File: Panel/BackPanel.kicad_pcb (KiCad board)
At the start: 2 copper layers, 0 parts

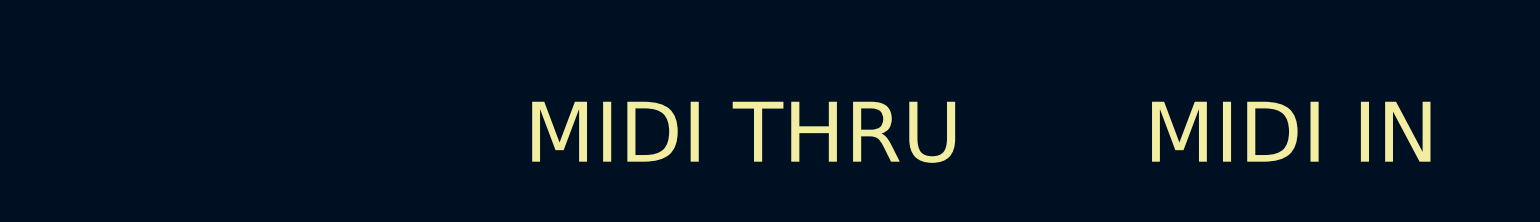
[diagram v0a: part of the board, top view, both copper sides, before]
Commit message: Exported DXFs, added more screw holes
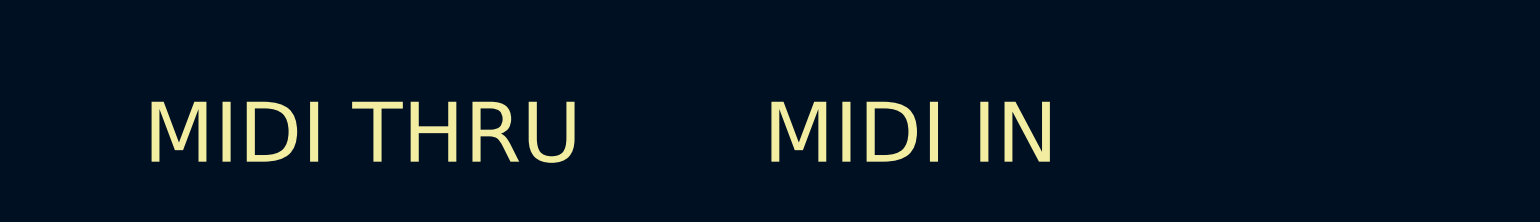
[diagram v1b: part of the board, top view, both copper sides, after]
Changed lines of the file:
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@@
   (general
     (thickness 1.6)
-    (drawings 23)
+    (drawings 26)
     (tracks 0)
     (zones 0)
@@
     (pad_to_mask_clearance 0.05)
     (aux_axis_origin 0 0)
+    (grid_origin 19.05 50.8)
     (visible_elements 7FFFFFFF)
     (pcbplotparams
-      (layerselection 0x010fc_ffffffff)
+      (layerselection 0x000a0_7ffffffe)
       (usegerberextensions false)
       (usegerberattributes true)
@@
       (padsonsilk false)
       (subtractmaskfromsilk false)
-      (outputformat 1)
+      (outputformat 3)
       (mirror false)
-      (drillshape 1)
+      (drillshape 0)
       (scaleselection 1)
-      (outputdirectory ""))
+      (outputdirectory "dxf/"))
   )
   (net 0 "")
@@
     (uvia_drill 0.1)
   )
-  (gr_text "MIDI THRU" (at 228.6 165.1) (layer F.SilkS)
+  (gr_circle (center 158.7 203.2) (end 160.7 203.2) (layer F.Mask) (width 0.15))
+  (gr_circle (center 279.35 203.2) (end 281.35 203.2) (layer F.Mask) (width 0.15))
+  (gr_circle (center 279.35 63.5) (end 281.35 63.5) (layer F.Mask) (width 0.15))
+  (gr_circle (center 527.05 63.5) (end 529.05 63.5) (layer F.Mask) (width 0.15))
+  (gr_circle (center 527.05 203.2) (end 529.05 203.2) (layer F.Mask) (width 0.15))
+  (gr_circle (center 31.75 201.7) (end 33.75 201.7) (layer F.Mask) (width 0.15))
+  (gr_circle (center 31.75 63.5) (end 33.75 63.5) (layer F.Mask) (width 0.15))
+  (gr_text "MIDI THRU" (at 196.85 165.1) (layer F.SilkS)
     (effects (font (size 5 5) (thickness 0.5)))
   )
-  (gr_text "MIDI IN" (at 274.32 165.1) (layer F.SilkS)
+  (gr_text "MIDI IN" (at 242.57 165.1) (layer F.SilkS)
     (effects (font (size 5 5) (thickness 0.5)))
   )
-  (gr_circle (center 239.85 180.34) (end 241.45 180.34) (layer F.Mask) (width 0.15))
-  (gr_circle (center 217.35 180.34) (end 218.95 180.34) (layer F.Mask) (width 0.15))
-  (gr_circle (center 228.6 180.34) (end 236.1 180.34) (layer F.Mask) (width 0.15))
-  (gr_circle (center 285.57 180.34) (end 287.17 180.34) (layer F.Mask) (width 0.15))
-  (gr_circle (center 263.07 180.34) (end 264.67 180.34) (layer F.Mask) (width 0.15))
-  (gr_circle (center 274.32 180.34) (end 281.82 180.34) (layer F.Mask) (width 0.15))
+  (gr_circle (center 208.1 180.34) (end 209.7 180.34) (layer F.Mask) (width 0.15))
+  (gr_circle (center 185.6 180.34) (end 187.2 180.34) (layer F.Mask) (width 0.15))
+  (gr_circle (center 196.85 180.34) (end 204.35 180.34) (layer F.Mask) (width 0.15))
+  (gr_circle (center 253.82 180.34) (end 255.42 180.34) (layer F.Mask) (width 0.15))
+  (gr_circle (center 231.32 180.34) (end 232.92 180.34) (layer F.Mask) (width 0.15))
+  (gr_circle (center 242.57 180.34) (end 250.07 180.34) (layer F.Mask) (width 0.15))
   (gr_circle (center 53.64 179.38) (end 55.39 179.38) (layer F.Mask) (width 0.15))
   (gr_circle (center 98.34 179.38) (end 100.09 179.38) (layer F.Mask) (width 0.15))
@@
     (effects (font (size 5 5) (thickness 0.5)))
   )
-  (gr_circle (center 527.05 63.5) (end 528.55 63.5) (layer F.Mask) (width 0.15))
-  (gr_circle (center 527.05 203.2) (end 528.55 203.2) (layer F.Mask) (width 0.15))
-  (gr_circle (center 31.75 201.7) (end 33.25 201.7) (layer F.Mask) (width 0.15))
-  (gr_circle (center 31.75 63.5) (end 33.25 63.5) (layer F.Mask) (width 0.15))
   (gr_line (start 19.05 215.9) (end 19.05 50.8) (layer F.Mask) (width 0.15))
   (gr_line (start 539.75 215.9) (end 19.05 215.9) (layer F.Mask) (width 0.15))

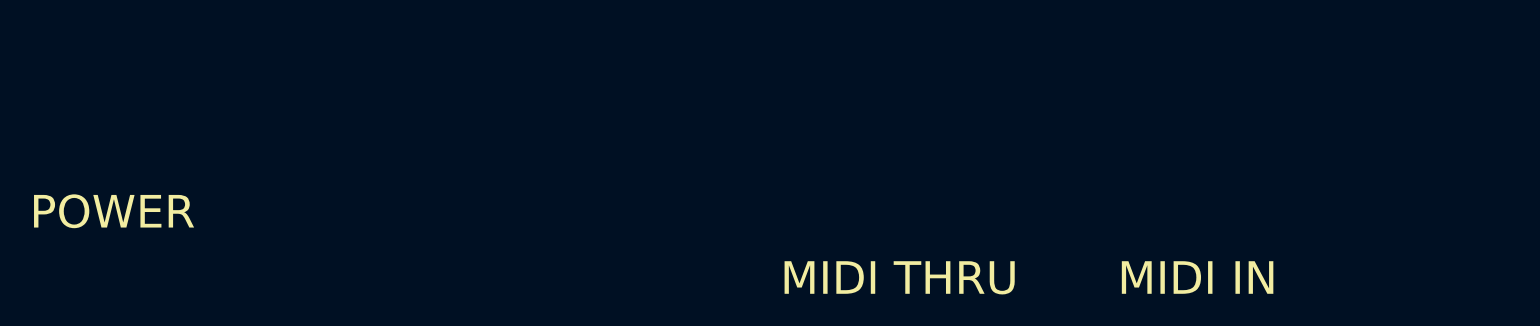
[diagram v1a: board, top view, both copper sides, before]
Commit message: Exported panel, fixed missing net on filter
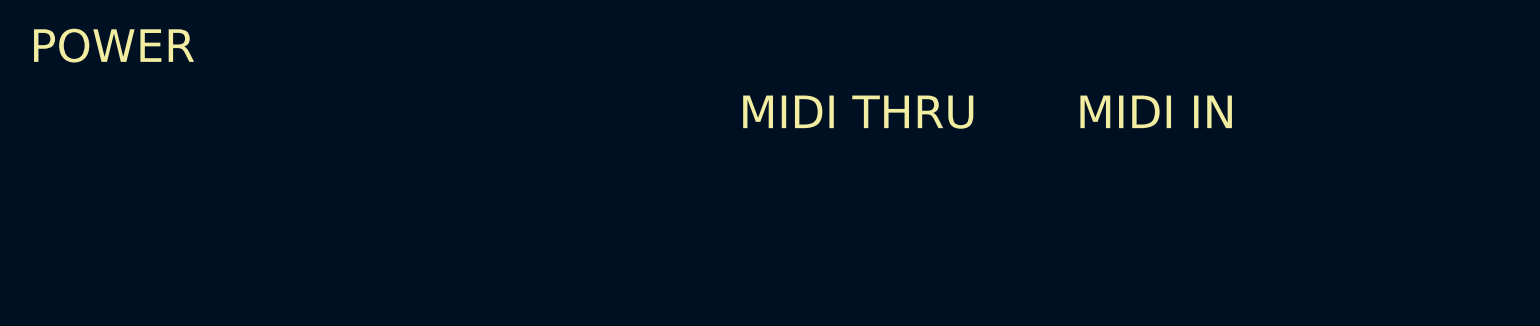
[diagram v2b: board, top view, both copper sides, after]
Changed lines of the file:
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@@
   (general
     (thickness 1.6)
-    (drawings 26)
+    (drawings 28)
     (tracks 0)
     (zones 0)
@@
       (padsonsilk false)
       (subtractmaskfromsilk false)
-      (outputformat 3)
+      (outputformat 5)
       (mirror false)
       (drillshape 0)
       (scaleselection 1)
-      (outputdirectory "dxf/"))
+      (outputdirectory "svg/"))
   )
   (net 0 "")
@@
     (uvia_drill 0.1)
   )
-  (gr_circle (center 158.7 203.2) (end 160.7 203.2) (layer F.Mask) (width 0.15))
-  (gr_circle (center 279.35 203.2) (end 281.35 203.2) (layer F.Mask) (width 0.15))
-  (gr_circle (center 279.35 63.5) (end 281.35 63.5) (layer F.Mask) (width 0.15))
+  (gr_circle (center 292.05 203.2) (end 294.05 203.2) (layer F.Mask) (width 0.15))
+  (gr_circle (center 292.05 63.5) (end 294.05 63.5) (layer F.Mask) (width 0.15))
+  (gr_circle (center 266.65 63.5) (end 268.65 63.5) (layer F.Mask) (width 0.15))
+  (gr_circle (center 266.65 203.2) (end 268.65 203.2) (layer F.Mask) (width 0.15))
+  (gr_circle (center 139.7 203.2) (end 141.7 203.2) (layer F.Mask) (width 0.15))
   (gr_circle (center 527.05 63.5) (end 529.05 63.5) (layer F.Mask) (width 0.15))
   (gr_circle (center 527.05 203.2) (end 529.05 203.2) (layer F.Mask) (width 0.15))
   (gr_circle (center 31.75 201.7) (end 33.75 201.7) (layer F.Mask) (width 0.15))
   (gr_circle (center 31.75 63.5) (end 33.75 63.5) (layer F.Mask) (width 0.15))
-  (gr_text "MIDI THRU" (at 196.85 165.1) (layer F.SilkS)
+  (gr_text "MIDI THRU" (at 190.5 139.7) (layer F.SilkS)
     (effects (font (size 5 5) (thickness 0.5)))
   )
-  (gr_text "MIDI IN" (at 242.57 165.1) (layer F.SilkS)
+  (gr_text "MIDI IN" (at 236.22 139.7) (layer F.SilkS)
     (effects (font (size 5 5) (thickness 0.5)))
   )
-  (gr_circle (center 208.1 180.34) (end 209.7 180.34) (layer F.Mask) (width 0.15))
-  (gr_circle (center 185.6 180.34) (end 187.2 180.34) (layer F.Mask) (width 0.15))
-  (gr_circle (center 196.85 180.34) (end 204.35 180.34) (layer F.Mask) (width 0.15))
-  (gr_circle (center 253.82 180.34) (end 255.42 180.34) (layer F.Mask) (width 0.15))
-  (gr_circle (center 231.32 180.34) (end 232.92 180.34) (layer F.Mask) (width 0.15))
-  (gr_circle (center 242.57 180.34) (end 250.07 180.34) (layer F.Mask) (width 0.15))
-  (gr_circle (center 53.64 179.38) (end 55.39 179.38) (layer F.Mask) (width 0.15))
-  (gr_circle (center 98.34 179.38) (end 100.09 179.38) (layer F.Mask) (width 0.15))
-  (gr_line (start 62.34 163.68) (end 62.34 195.08) (layer F.Mask) (width 0.15))
-  (gr_line (start 89.64 163.68) (end 62.34 163.68) (layer F.Mask) (width 0.15))
-  (gr_line (start 89.64 195.08) (end 89.64 163.68) (layer F.Mask) (width 0.15))
-  (gr_line (start 62.34 195.08) (end 89.64 195.08) (layer F.Mask) (width 0.15))
-  (gr_text POWER (at 76.2 154.94) (layer F.SilkS)
+  (gr_circle (center 201.75 154.94) (end 203.35 154.94) (layer F.Mask) (width 0.15))
+  (gr_circle (center 179.25 154.94) (end 180.85 154.94) (layer F.Mask) (width 0.15))
+  (gr_circle (center 190.5 154.94) (end 198 154.94) (layer F.Mask) (width 0.15))
+  (gr_circle (center 247.47 154.94) (end 249.07 154.94) (layer F.Mask) (width 0.15))
+  (gr_circle (center 224.97 154.94) (end 226.57 154.94) (layer F.Mask) (width 0.15))
+  (gr_circle (center 236.22 154.94) (end 243.72 154.94) (layer F.Mask) (width 0.15))
+  (gr_circle (center 53.64 153.98) (end 55.39 153.98) (layer F.Mask) (width 0.15))
+  (gr_circle (center 98.34 153.98) (end 100.09 153.98) (layer F.Mask) (width 0.15))
+  (gr_line (start 62.34 138.28) (end 62.34 169.68) (layer F.Mask) (width 0.15))
+  (gr_line (start 89.64 138.28) (end 62.34 138.28) (layer F.Mask) (width 0.15))
+  (gr_line (start 89.64 169.68) (end 89.64 138.28) (layer F.Mask) (width 0.15))
+  (gr_line (start 62.34 169.68) (end 89.64 169.68) (layer F.Mask) (width 0.15))
+  (gr_text POWER (at 76.2 129.54) (layer F.SilkS)
     (effects (font (size 5 5) (thickness 0.5)))
   )

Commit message: Added panel dimensions, changed Perc Volume pot
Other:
- board text added: "3.2mm"
- board text added: "3.5mm"
- board text added: "4mm"
